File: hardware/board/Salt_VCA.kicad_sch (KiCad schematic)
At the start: 37 parts, among them Q701 BCM847, U5 TL074

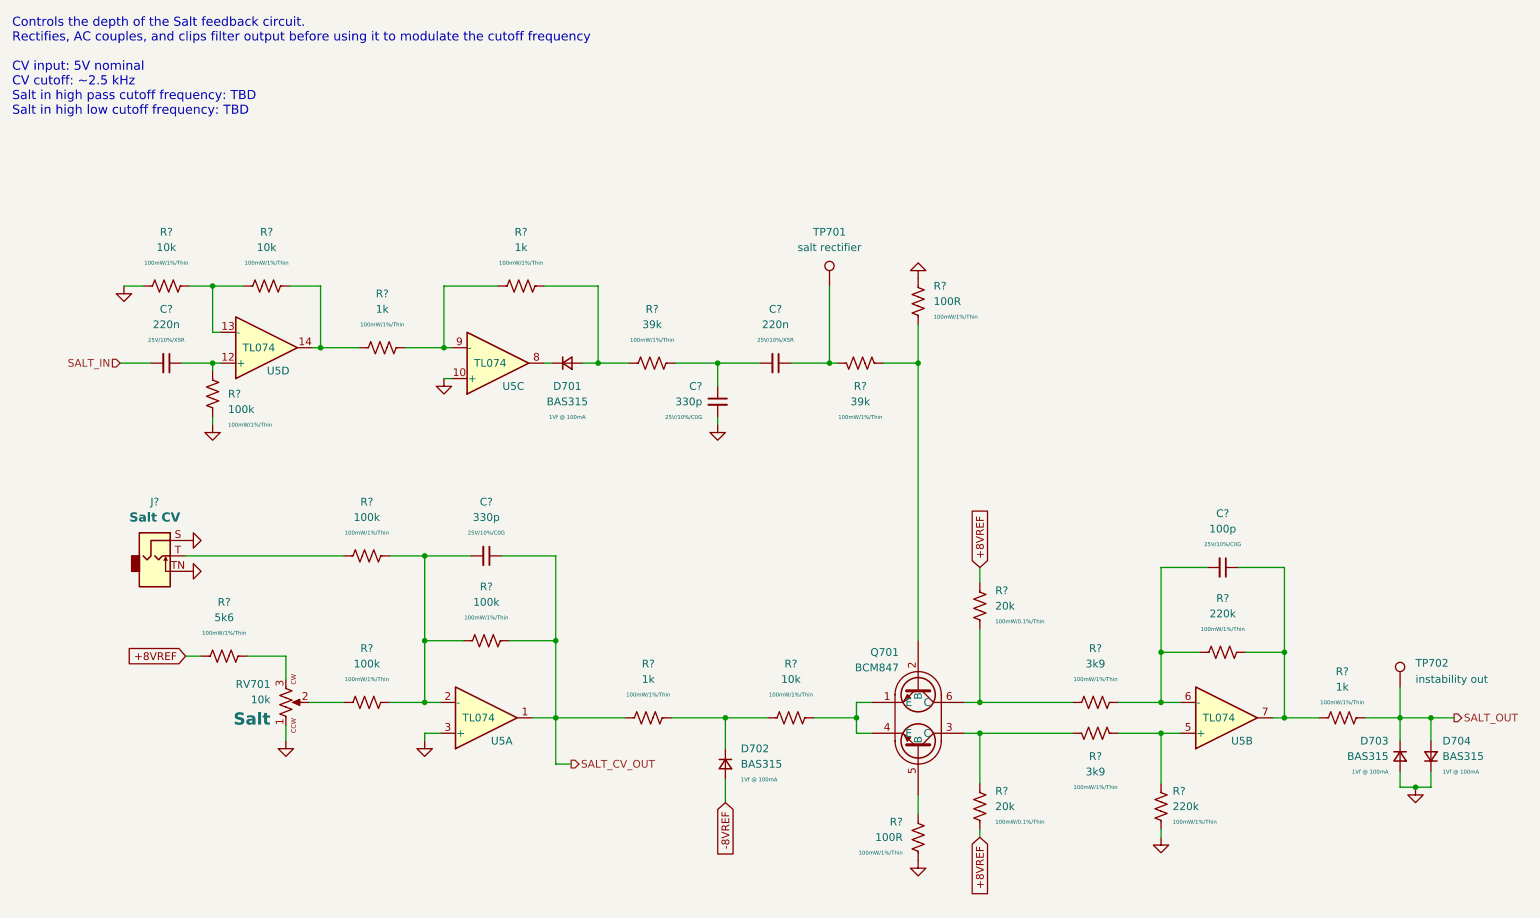
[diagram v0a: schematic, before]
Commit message: update board to kicad 9
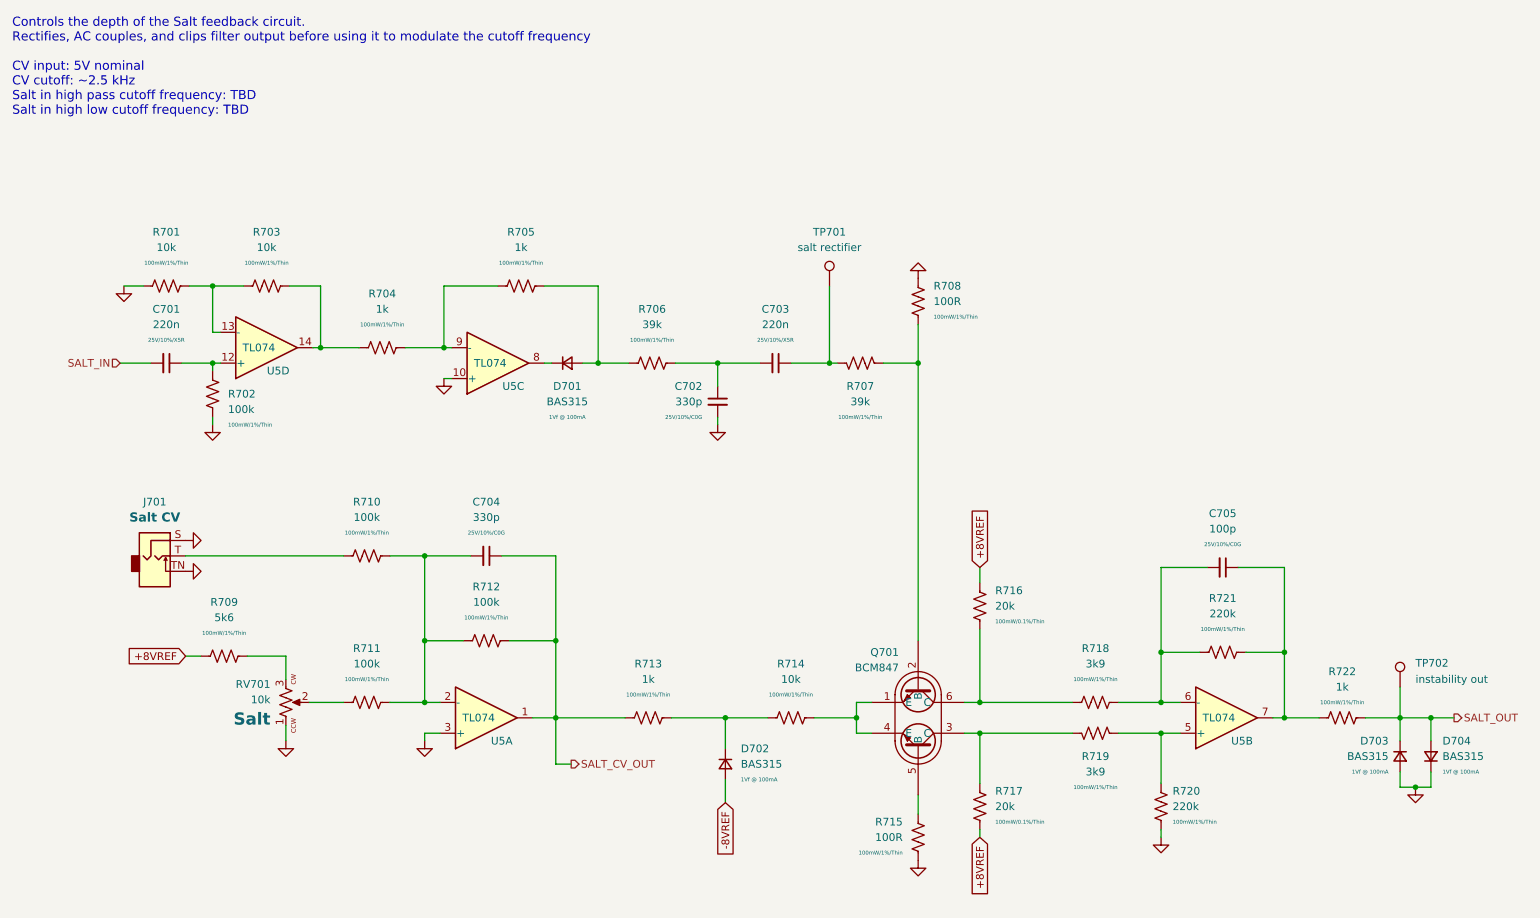
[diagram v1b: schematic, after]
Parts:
- gave numbers to parts that had none: 28

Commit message: remove test points from BOM
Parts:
- TP701, TP702: now left out of the parts list
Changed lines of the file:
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@@
 		(unit 1)
 		(exclude_from_sim no)
-		(in_bom yes)
+		(in_bom no)
 		(on_board yes)
 		(dnp no)
@@
 		(unit 1)
 		(exclude_from_sim no)
-		(in_bom yes)
+		(in_bom no)
 		(on_board yes)
 		(dnp no)
